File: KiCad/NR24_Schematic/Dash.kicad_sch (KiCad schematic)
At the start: 11 parts, among them J9 AEM Dash, SW1 GLVMS, SW2 Shifter Switch, SW5 Key Switch, SW6 12V E-stop

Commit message: dash fix
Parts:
- SW1: value GLVMS -> TI power switch
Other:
- note removed: "independent CAN watchdoggy device"

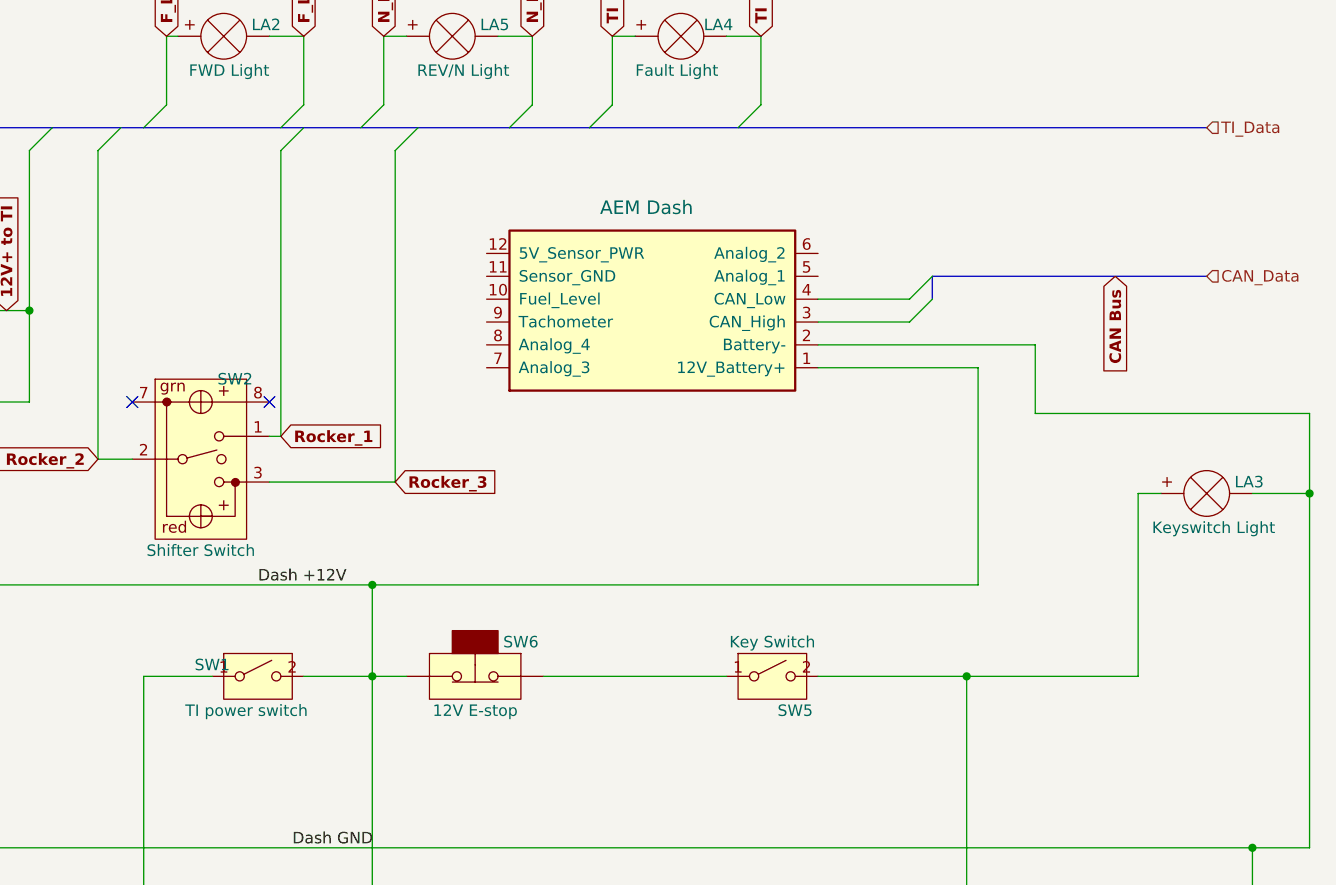
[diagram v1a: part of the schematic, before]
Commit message: AMS with relay
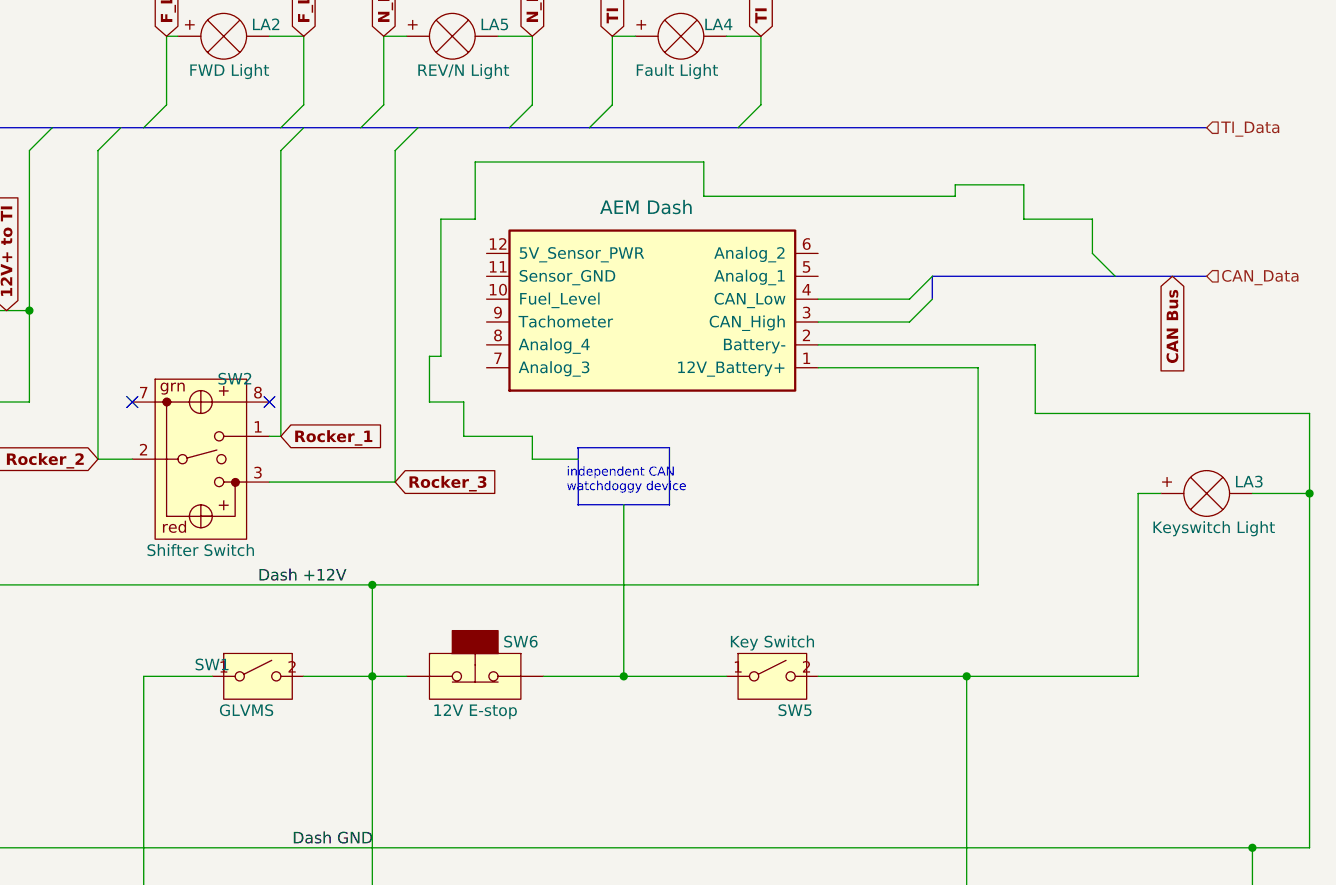
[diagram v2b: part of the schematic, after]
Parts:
- SW1: value TI power switch -> GLVMS
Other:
- note added: "independent CAN watchdoggy device"
